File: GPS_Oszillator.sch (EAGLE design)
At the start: 33 parts, among them IC1 74ACT04D, IC2 7805TV, X1 ST-SMB-V, X2 ST-SMB-V

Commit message: Add files via upload
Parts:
- removed JP1: to_PB6, pinhead:PINHD-1X2
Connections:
- removed net N$1: IC1A.O, R3.2
- removed net RESET: U$2.RST
- new net PPS_IN: IC1A.O, R3.2, U$4.34
- new net PWM_OUT: IC1E.I, U$4.32
- new net RST: U$2.RST, U$4.17
- net 10MHZ_IN: now also U$4.35; no longer JP1.1
- net DC: now also U$4.16
- net GND: no longer IC1E.I, JP1.2
- net PWM_16BIT: now also IC1E.O
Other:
- moved on the sheet: IC1E
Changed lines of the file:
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@@
 <part name="SUPPLY1" library="supply2" deviceset="GND" device=""/>
 <part name="IC2" library="linear" deviceset="78*" device="TV" technology="05"/>
-<part name="JP1" library="pinhead" deviceset="PINHD-1X2" device="" value="to_PB6"/>
-<part name="SUPPLY3" library="supply2" deviceset="GND" device=""/>
 <part name="JP2" library="pinhead" deviceset="PINHD-1X2" device="" value="10M_OUT"/>
 <part name="SUPPLY4" library="supply2" deviceset="GND" device=""/>
@@
 <part name="SUPPLY26" library="supply2" deviceset="GND" device=""/>
 <part name="SUPPLY25" library="supply2" deviceset="GND" device=""/>
-<part name="SUPPLY27" library="supply2" deviceset="GND" device=""/>
 <part name="D1" library="diode" deviceset="1N4004" device=""/>
 <part name="SUPPLY28" library="supply2" deviceset="GND" device=""/>
@@
 <instance part="IC1" gate="C" x="-68.58" y="33.02" rot="R180"/>
 <instance part="IC1" gate="D" x="-68.58" y="17.78" rot="R180"/>
-<instance part="IC1" gate="E" x="198.12" y="88.9"/>
+<instance part="IC1" gate="E" x="-25.4" y="66.04" rot="MR0"/>
 <instance part="IC1" gate="F" x="198.12" y="76.2"/>
 <instance part="IC1" gate="P" x="144.78" y="86.36"/>
@@
 <instance part="SUPPLY1" gate="GND" x="-81.28" y="73.66"/>
 <instance part="IC2" gate="A1" x="114.3" y="93.98"/>
-<instance part="JP1" gate="G$1" x="-66.04" y="76.2" smashed="yes">
-<attribute name="NAME" x="-62.23" y="79.375" size="1.778" layer="95"/>
-<attribute name="VALUE" x="-62.23" y="76.2" size="1.778" layer="96"/>
-</instance>
-<instance part="SUPPLY3" gate="GND" x="-68.58" y="73.66"/>
 <instance part="JP2" gate="G$1" x="-86.36" y="48.26" smashed="yes" rot="MR0">
 <attribute name="NAME" x="-92.71" y="48.895" size="1.778" layer="95" rot="MR0"/>
@@
 <instance part="SUPPLY26" gate="GND" x="73.66" y="86.36"/>
 <instance part="SUPPLY25" gate="GND" x="187.96" y="73.66"/>
-<instance part="SUPPLY27" gate="GND" x="187.96" y="86.36"/>
 <instance part="D1" gate="1" x="81.28" y="91.44" rot="R90"/>
 <instance part="SUPPLY28" gate="GND" x="81.28" y="86.36"/>
@@
 </segment>
 <segment>
-<pinref part="JP1" gate="G$1" pin="2"/>
-<pinref part="SUPPLY3" gate="GND" pin="GND"/>
-</segment>
-<segment>
 <pinref part="JP2" gate="G$1" pin="2"/>
 <pinref part="SUPPLY4" gate="GND" pin="GND"/>
@@
 </segment>
 <segment>
-<pinref part="IC1" gate="E" pin="I"/>
-<pinref part="SUPPLY27" gate="GND" pin="GND"/>
-</segment>
-<segment>
 <pinref part="D1" gate="1" pin="A"/>
 <pinref part="SUPPLY28" gate="GND" pin="GND"/>
@@
 </segment>
 </net>
-<net name="N$1" class="0">
+<net name="PPS_IN" class="0">
 <segment>
 <pinref part="IC1" gate="A" pin="O"/>
 <wire x1="-55.88" y1="96.52" x2="-48.26" y2="96.52" width="0.1524" layer="91"/>
 <wire x1="-48.26" y1="96.52" x2="-43.18" y2="96.52" width="0.1524" layer="91"/>
-<wire x1="-43.18" y1="96.52" x2="-43.18" y2="66.04" width="0.1524" layer="91"/>
-<wire x1="-43.18" y1="66.04" x2="-12.7" y2="66.04" width="0.1524" layer="91"/>
+<wire x1="-43.18" y1="96.52" x2="-43.18" y2="73.66" width="0.1524" layer="91"/>
 <pinref part="R3" gate="G$1" pin="2"/>
 <junction x="-48.26" y="96.52"/>
+<pinref part="U$4" gate="G$1" pin="34"/>
+<wire x1="0" y1="73.66" x2="-43.18" y2="73.66" width="0.1524" layer="91"/>
+<label x="-10.16" y="73.66" size="1.778" layer="95"/>
 </segment>
 </net>
@@
 <segment>
 <pinref part="X1" gate="G1" pin="1"/>
-<pinref part="JP1" gate="G$1" pin="1"/>
-<wire x1="-81.28" y1="78.74" x2="-76.2" y2="78.74" width="0.1524" layer="91"/>
-<wire x1="-76.2" y1="78.74" x2="-68.58" y2="78.74" width="0.1524" layer="91"/>
-<wire x1="-76.2" y1="78.74" x2="-76.2" y2="60.96" width="0.1524" layer="91"/>
-<wire x1="-76.2" y1="60.96" x2="-53.34" y2="60.96" width="0.1524" layer="91"/>
-<wire x1="-53.34" y1="60.96" x2="-53.34" y2="50.8" width="0.1524" layer="91"/>
+<wire x1="-81.28" y1="78.74" x2="-53.34" y2="78.74" width="0.1524" layer="91"/>
+<wire x1="-53.34" y1="78.74" x2="-53.34" y2="71.12" width="0.1524" layer="91"/>
 <pinref part="IC1" gate="B" pin="I"/>
+<wire x1="-53.34" y1="71.12" x2="-53.34" y2="50.8" width="0.1524" layer="91"/>
 <wire x1="-53.34" y1="50.8" x2="-58.42" y2="50.8" width="0.1524" layer="91"/>
-<junction x="-76.2" y="78.74"/>
+<pinref part="U$4" gate="G$1" pin="35"/>
+<wire x1="0" y1="71.12" x2="-53.34" y2="71.12" width="0.1524" layer="91"/>
+<junction x="-53.34" y="71.12"/>
+<label x="-12.7" y="71.12" size="1.778" layer="95"/>
 </segment>
 </net>
@@
 <segment>
 <pinref part="R1" gate="G$1" pin="2"/>
-<wire x1="-43.18" y1="-7.62" x2="-43.18" y2="45.72" width="0.1524" layer="91"/>
-<wire x1="-12.7" y1="45.72" x2="-43.18" y2="45.72" width="0.1524" layer="91"/>
+<wire x1="-43.18" y1="-7.62" x2="-43.18" y2="66.04" width="0.1524" layer="91"/>
+<wire x1="-35.56" y1="66.04" x2="-43.18" y2="66.04" width="0.1524" layer="91"/>
 <label x="-43.18" y="7.62" size="1.778" layer="95" rot="R90"/>
+<pinref part="IC1" gate="E" pin="O"/>
 </segment>
 </net>
@@
 </segment>
 </net>
-<net name="RESET" class="0">
-<segment>
-<wire x1="-12.7" y1="50.8" x2="-27.94" y2="50.8" width="0.1524" layer="91"/>
-<wire x1="-27.94" y1="50.8" x2="-27.94" y2="30.48" width="0.1524" layer="91"/>
-<wire x1="-27.94" y1="30.48" x2="101.6" y2="30.48" width="0.1524" layer="91"/>
-<label x="38.1" y="30.48" size="1.778" layer="95"/>
+<net name="RST" class="0">
+<segment>
+<wire x1="91.44" y1="30.48" x2="101.6" y2="30.48" width="0.1524" layer="91"/>
 <pinref part="U$2" gate="G$1" pin="RST"/>
+<label x="93.98" y="30.48" size="1.778" layer="95"/>
+</segment>
+<segment>
+<wire x1="30.48" y1="58.42" x2="40.64" y2="58.42" width="0.1524" layer="91"/>
+<label x="33.02" y="58.42" size="1.778" layer="95"/>
+<pinref part="U$4" gate="G$1" pin="17"/>
 </segment>
 </net>
 <net name="DC" class="0">
 <segment>
-<wire x1="-12.7" y1="48.26" x2="-25.4" y2="48.26" width="0.1524" layer="91"/>
-<wire x1="-25.4" y1="48.26" x2="-25.4" y2="25.4" width="0.1524" layer="91"/>
-<wire x1="-25.4" y1="25.4" x2="101.6" y2="25.4" width="0.1524" layer="91"/>
-<label x="40.64" y="25.4" size="1.778" layer="95"/>
+<wire x1="91.44" y1="25.4" x2="101.6" y2="25.4" width="0.1524" layer="91"/>
 <pinref part="U$2" gate="G$1" pin="AO"/>
+<label x="93.98" y="25.4" size="1.778" layer="95"/>
+</segment>
+<segment>
+<wire x1="30.48" y1="55.88" x2="40.64" y2="55.88" width="0.1524" layer="91"/>
+<label x="33.02" y="55.88" size="1.778" layer="95"/>
+<pinref part="U$4" gate="G$1" pin="16"/>
 </segment>
 </net>
@@
 </segment>
 </net>
+<net name="PWM_OUT" class="0">
+<segment>
+<pinref part="IC1" gate="E" pin="I"/>
+<wire x1="-15.24" y1="66.04" x2="-15.24" y2="68.58" width="0.1524" layer="91"/>
+<pinref part="U$4" gate="G$1" pin="32"/>
+<wire x1="-15.24" y1="68.58" x2="0" y2="68.58" width="0.1524" layer="91"/>
+<label x="-12.7" y="68.58" size="1.778" layer="95"/>
+</segment>
+</net>

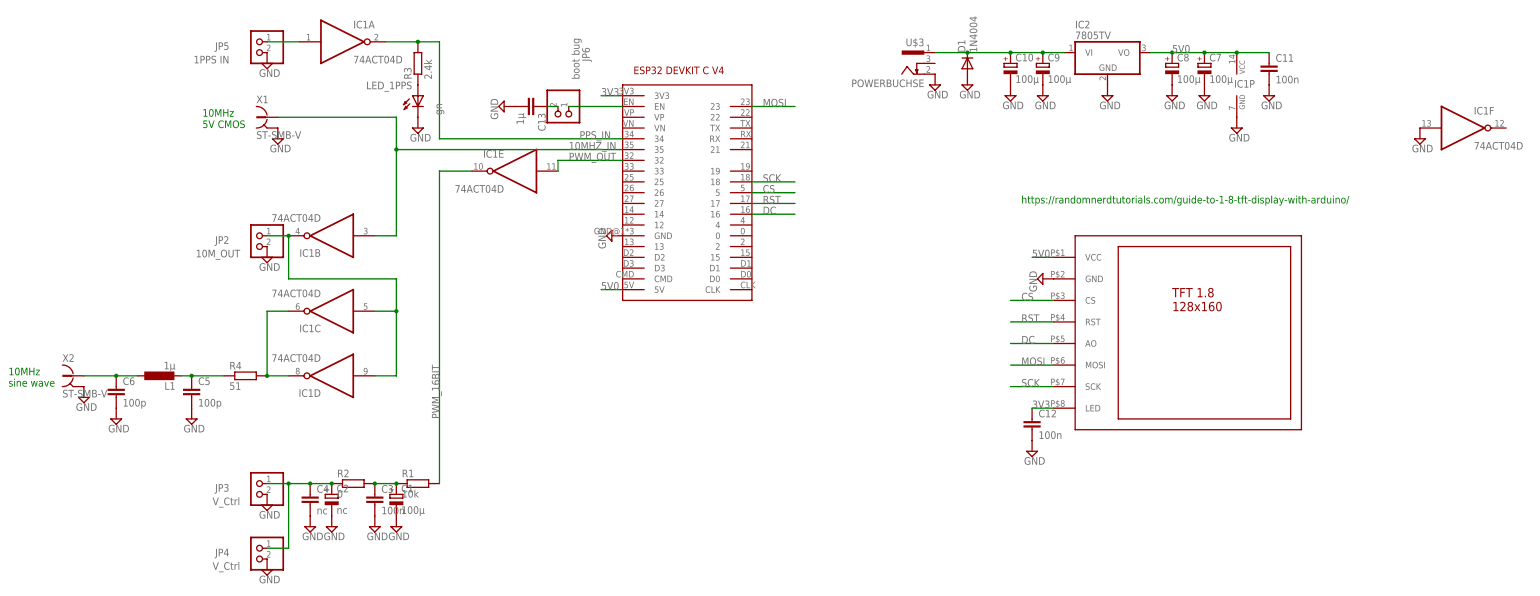
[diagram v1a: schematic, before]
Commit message: Change PWM filter
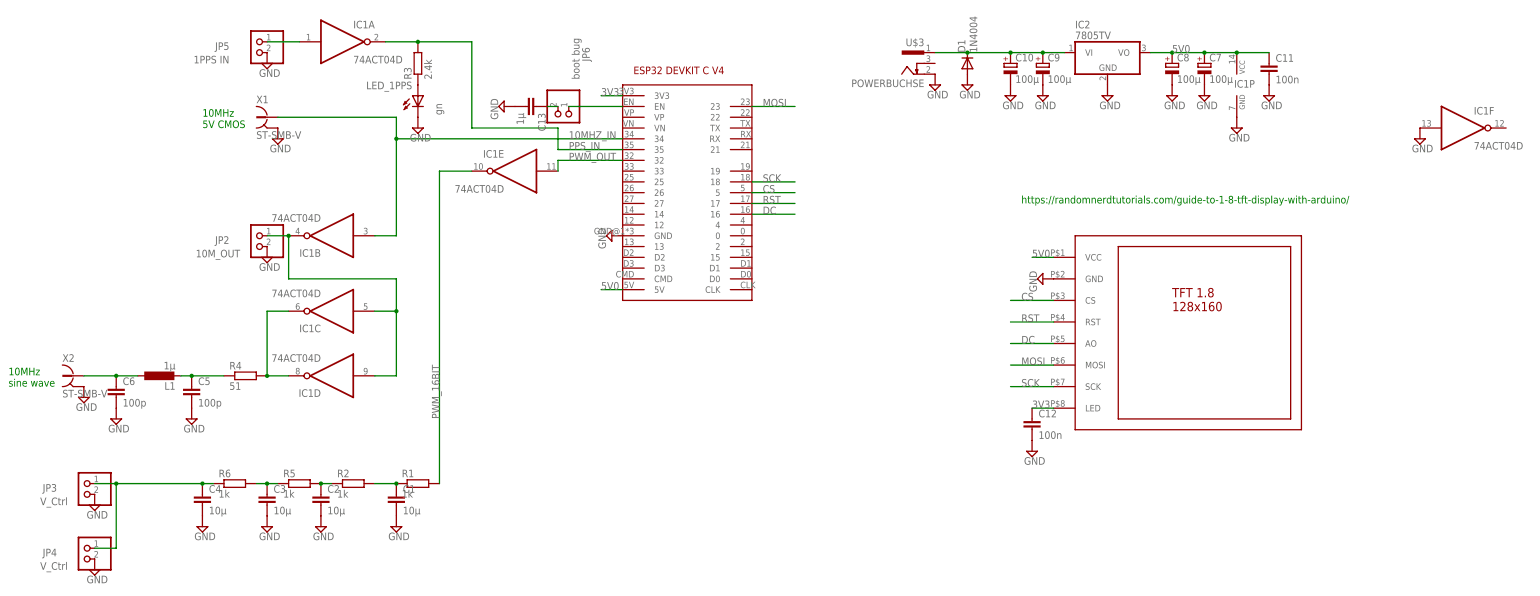
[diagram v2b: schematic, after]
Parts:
- added R5, R6: 1k, rcl:R-EU_R0805
- C1: value 100µ -> 10µ; device rcl:CPOL-EUSANYO_SMD_E7 -> rcl:C-EUC1206
- C2: value nc -> 10µ; device rcl:CPOL-EUSANYO_SMD_E7 -> rcl:C-EUC1206
- C3: value 100n -> 10µ; device rcl:C-EUC0805 -> rcl:C-EUC1206
- C4: value nc -> 10µ; device rcl:C-EUC0805 -> rcl:C-EUC1206
- R1: value 10k -> 1k
- R2: value 0 -> 1k
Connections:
- new net N$1: C3.1, R5.1, R6.2
- new net N$3: C2.1, R2.1, R5.2
- net 10MHZ_IN: now also U$4.34; no longer U$4.35
- net GND: now also C1.2, C2.2; no longer C1.-, C2.-
- net N$5: now also C1.1; no longer C1.+, C3.1
- net N$6: now also R6.1; no longer C2.+, R2.1
- net PPS_IN: now also U$4.35; no longer U$4.34
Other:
- moved on the sheet: C3, C4, JP3, JP4

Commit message: update esp32 inputs.
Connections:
- net 10MHZ_IN: now also U$4.4; no longer U$4.34
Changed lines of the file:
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@@
 <setting verticaltext="up"/>
 </settings>
-<grid distance="0.1" unitdist="inch" unit="inch" style="lines" multiple="1" display="no" altdistance="0.01" altunitdist="inch" altunit="inch"/>
+<grid distance="25" unitdist="mil" unit="mil" style="lines" multiple="1" display="no" altdistance="0.01" altunitdist="inch" altunit="inch"/>
 <layers>
 <layer number="1" name="Top" color="4" fill="1" visible="no" active="no"/>
@@
 <attribute name="VALUE" x="-10.16" y="87.63" size="1.778" layer="96" rot="R90"/>
 </instance>
-<instance part="U$4" gate="G$1" x="17.78" y="60.96"/>
+<instance part="U$4" gate="G$1" x="19.05" y="60.96"/>
 <instance part="SUPPLY30" gate="GND" x="-2.54" y="50.8" rot="R270"/>
 <instance part="R2" gate="G$1" x="-63.5" y="-7.62"/>
@@
 <pinref part="U$4" gate="G$1" pin="GND"/>
 <pinref part="SUPPLY30" gate="GND" pin="GND"/>
+<wire x1="1.27" y1="50.8" x2="0" y2="50.8" width="0.1524" layer="91"/>
 </segment>
 <segment>
@@
 <label x="-12.7" y="71.12" size="1.778" layer="95"/>
 <pinref part="U$4" gate="G$1" pin="35"/>
-<wire x1="0" y1="71.12" x2="-15.24" y2="71.12" width="0.1524" layer="91"/>
+<wire x1="1.27" y1="71.12" x2="-15.24" y2="71.12" width="0.1524" layer="91"/>
 <wire x1="-15.24" y1="71.12" x2="-15.24" y2="76.2" width="0.1524" layer="91"/>
 <wire x1="-15.24" y1="76.2" x2="-35.56" y2="76.2" width="0.1524" layer="91"/>
@@
 <wire x1="-53.34" y1="73.66" x2="-53.34" y2="50.8" width="0.1524" layer="91"/>
 <wire x1="-53.34" y1="50.8" x2="-58.42" y2="50.8" width="0.1524" layer="91"/>
-<wire x1="0" y1="73.66" x2="-53.34" y2="73.66" width="0.1524" layer="91"/>
 <junction x="-53.34" y="73.66"/>
-<label x="-12.7" y="73.66" size="1.778" layer="95"/>
-<pinref part="U$4" gate="G$1" pin="34"/>
+<label x="-38.1" y="73.66" size="1.778" layer="95"/>
+<wire x1="-5.08" y1="73.66" x2="-53.34" y2="73.66" width="0.1524" layer="91"/>
+<wire x1="22.86" y1="53.34" x2="22.86" y2="30.48" width="0.1524" layer="91"/>
+<wire x1="22.86" y1="30.48" x2="-5.08" y2="30.48" width="0.1524" layer="91"/>
+<wire x1="-5.08" y1="30.48" x2="-5.08" y2="73.66" width="0.1524" layer="91"/>
+<wire x1="31.75" y1="53.34" x2="22.86" y2="53.34" width="0.1524" layer="91"/>
+<pinref part="U$4" gate="G$1" pin="4"/>
 </segment>
 </net>
@@
 </segment>
 <segment>
-<wire x1="0" y1="38.1" x2="-5.08" y2="38.1" width="0.1524" layer="91"/>
+<wire x1="1.27" y1="38.1" x2="-5.08" y2="38.1" width="0.1524" layer="91"/>
 <label x="-5.08" y="38.1" size="1.778" layer="95"/>
 <pinref part="U$4" gate="G$1" pin="5V"/>
@@
 </segment>
 <segment>
-<wire x1="0" y1="83.82" x2="-5.08" y2="83.82" width="0.1524" layer="91"/>
+<wire x1="1.27" y1="83.82" x2="-5.08" y2="83.82" width="0.1524" layer="91"/>
 <label x="-5.08" y="83.82" size="1.778" layer="95"/>
 <pinref part="U$4" gate="G$1" pin="3V3"/>
@@
 </segment>
 <segment>
-<wire x1="40.64" y1="63.5" x2="30.48" y2="63.5" width="0.1524" layer="91"/>
+<wire x1="40.64" y1="63.5" x2="31.75" y2="63.5" width="0.1524" layer="91"/>
 <label x="33.02" y="63.5" size="1.778" layer="95"/>
 <pinref part="U$4" gate="G$1" pin="18"/>
@@
 </segment>
 <segment>
-<wire x1="40.64" y1="81.28" x2="30.48" y2="81.28" width="0.1524" layer="91"/>
+<wire x1="40.64" y1="81.28" x2="31.75" y2="81.28" width="0.1524" layer="91"/>
 <label x="33.02" y="81.28" size="1.778" layer="95"/>
 <pinref part="U$4" gate="G$1" pin="23"/>
@@
 </segment>
 <segment>
-<wire x1="30.48" y1="58.42" x2="40.64" y2="58.42" width="0.1524" layer="91"/>
+<wire x1="31.75" y1="58.42" x2="40.64" y2="58.42" width="0.1524" layer="91"/>
 <label x="33.02" y="58.42" size="1.778" layer="95"/>
 <pinref part="U$4" gate="G$1" pin="17"/>
@@
 </segment>
 <segment>
-<wire x1="30.48" y1="55.88" x2="40.64" y2="55.88" width="0.1524" layer="91"/>
+<wire x1="31.75" y1="55.88" x2="40.64" y2="55.88" width="0.1524" layer="91"/>
 <label x="33.02" y="55.88" size="1.778" layer="95"/>
 <pinref part="U$4" gate="G$1" pin="16"/>
@@
 </segment>
 <segment>
-<wire x1="30.48" y1="60.96" x2="40.64" y2="60.96" width="0.1524" layer="91"/>
+<wire x1="31.75" y1="60.96" x2="40.64" y2="60.96" width="0.1524" layer="91"/>
 <label x="33.02" y="60.96" size="1.778" layer="95"/>
 <pinref part="U$4" gate="G$1" pin="5"/>
@@
 <pinref part="JP6" gate="G$1" pin="1"/>
 <pinref part="U$4" gate="G$1" pin="EN"/>
-<wire x1="0" y1="81.28" x2="-12.7" y2="81.28" width="0.1524" layer="91"/>
+<wire x1="1.27" y1="81.28" x2="-12.7" y2="81.28" width="0.1524" layer="91"/>
 </segment>
 </net>
@@
 <wire x1="-15.24" y1="66.04" x2="-15.24" y2="68.58" width="0.1524" layer="91"/>
 <pinref part="U$4" gate="G$1" pin="32"/>
-<wire x1="-15.24" y1="68.58" x2="0" y2="68.58" width="0.1524" layer="91"/>
+<wire x1="-15.24" y1="68.58" x2="1.27" y2="68.58" width="0.1524" layer="91"/>
 <label x="-12.7" y="68.58" size="1.778" layer="95"/>
 </segment>
